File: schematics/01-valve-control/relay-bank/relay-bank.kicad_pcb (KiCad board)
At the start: 4 copper layers, 68.8 x 86.5 mm, 40 parts, among them J102 PWR, J201 VALVE, J301 VALVE, J401 VALVE, J501 VALVE, J601 VALVE, K201 SPST Relay, K301 SPST Relay, K401 SPST Relay, K501 SPST Relay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

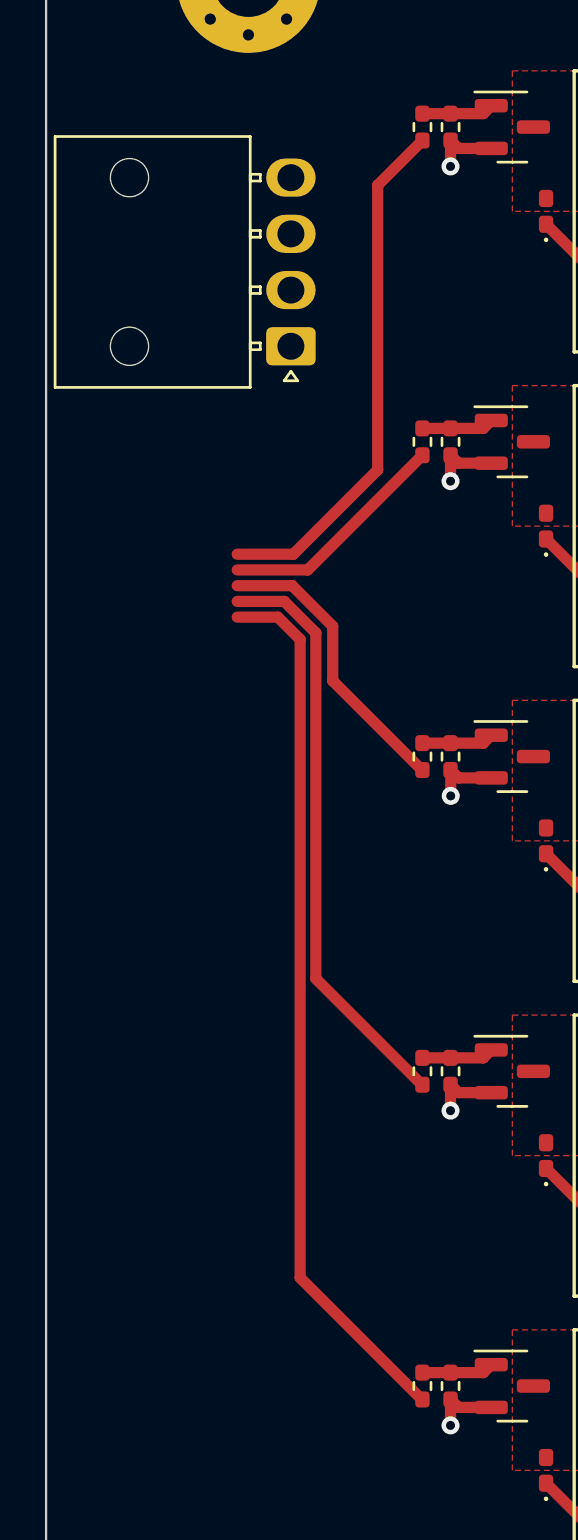
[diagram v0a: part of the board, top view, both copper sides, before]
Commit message: Add connector for valve control enable inputs
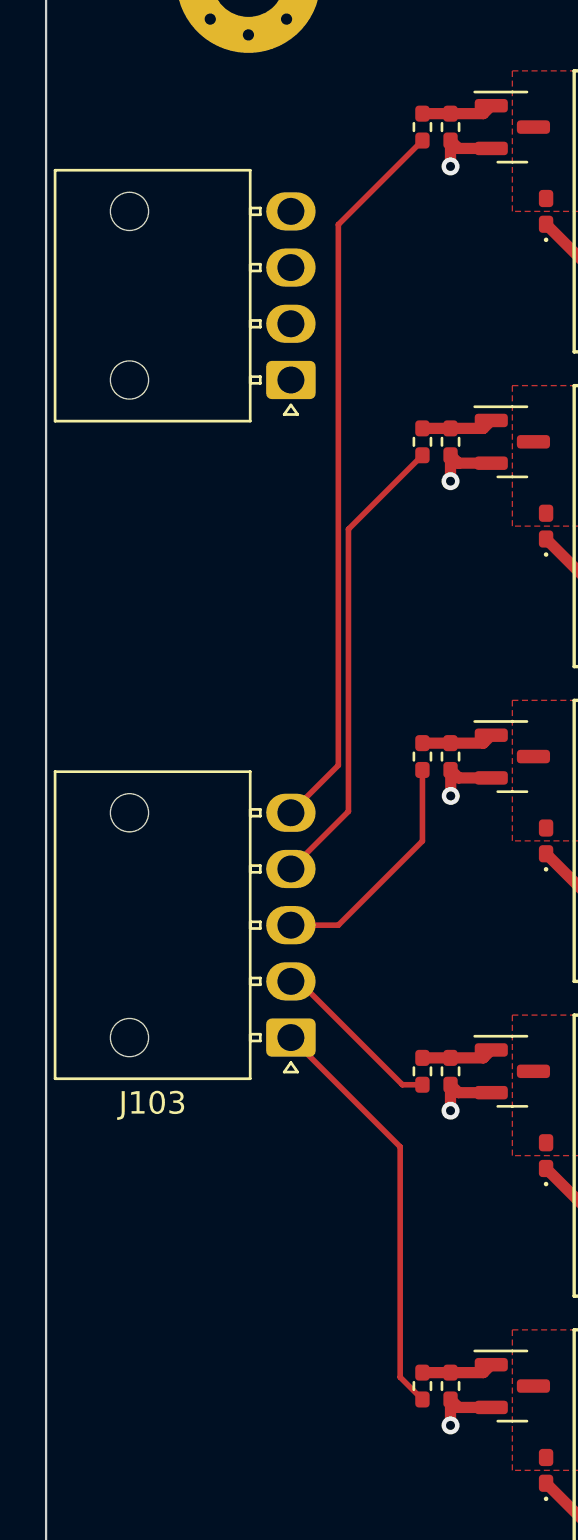
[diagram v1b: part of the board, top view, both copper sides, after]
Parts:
- added J103: EN, royale:Molex_Nano-Fit_105313-xx05_1x05_P2.50mm_Horizontal, F.Cu at (133.9, 118.5)
- moved J102 1.50 mm to (133.9, 89.2)
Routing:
- net /EN_01: track 39.3 -> 18.5 mm
- net /EN_02: track 26.2 -> 7.75 mm
- net /EN_04: track 10.4 -> 20.8 mm
- net /EN_05: track 23.3 -> 32.3 mm
- net /EN_03: track 13.1 -> 10.6 mm
